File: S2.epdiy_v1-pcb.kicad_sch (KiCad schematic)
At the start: 87 parts, among them J1 USB_C_Receptacle_USB2.0, J2 Jack-DC, P1 CONN_02X13, SW1 RESET, SW2 BOOT, U1 MCP1700-1202E_SOT23, U11 TP4056, U2 ESP32-S2-WROVER, U3 QFN50P700X700X100-49N, U6 ED060XC5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

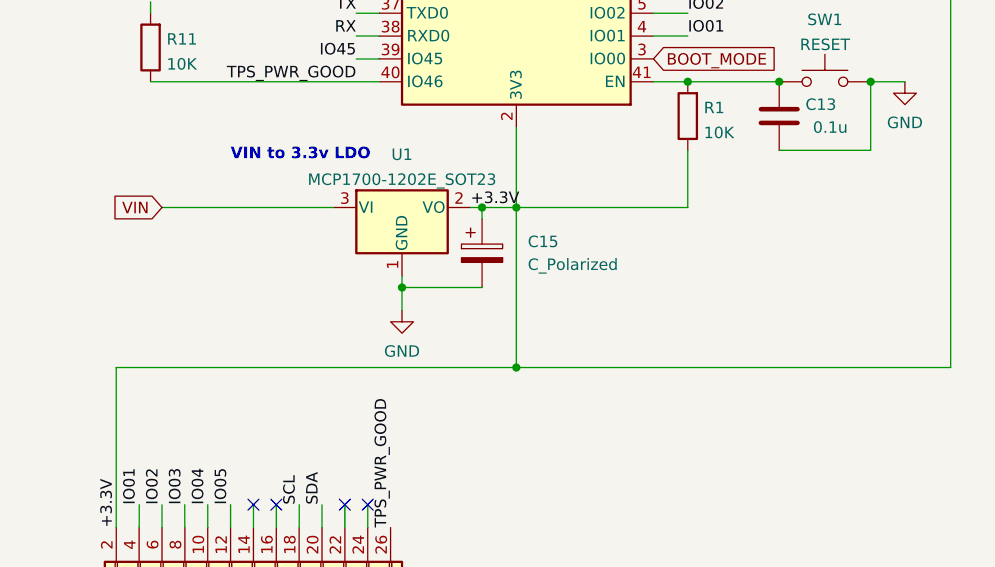
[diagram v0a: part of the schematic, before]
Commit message: Update LDO caps
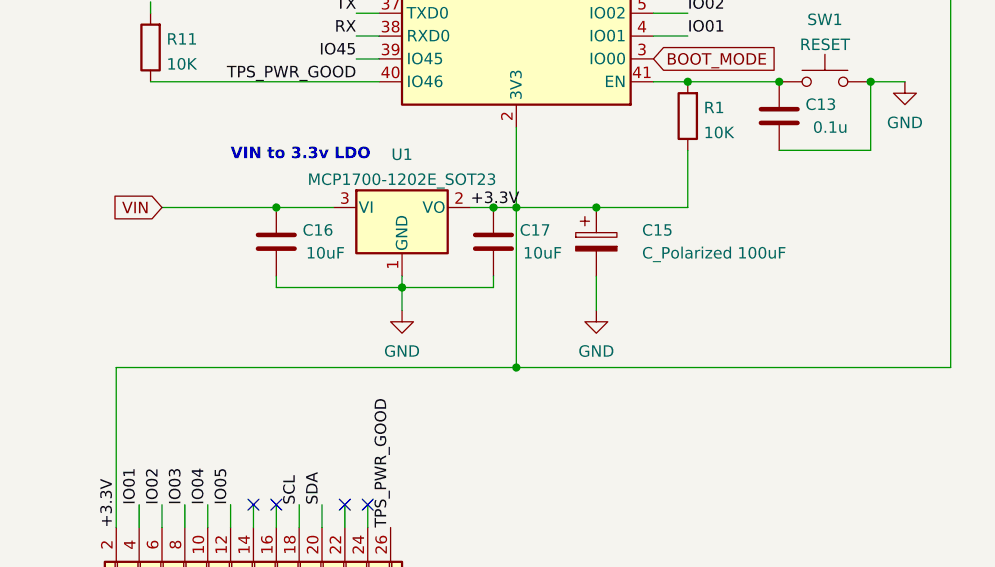
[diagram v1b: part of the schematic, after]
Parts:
- added C16, C17: 10uF, Capacitor_SMD:C_0805_2012Metric, symbol Device:C
- C15: value C_Polarized -> C_Polarized 100uF; footprint Capacitor_Tantalum_SMD:CP_EIA-7343-43_Kemet-X -> Capacitor_Tantalum_SMD:CP_EIA-3528-21_Kemet-B; LCSC C513339 -> C129289
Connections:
- net +3.3V: now also C17.1
- net GND: now also C16.2, C17.2
- net SW_VIN: now also C16.1
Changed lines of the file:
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@@
   (junction (at 309.88 226.06) (diameter 0) (color 0 0 0 0)
   )
+  (junction (at 129.54 105.41) (diameter 0) (color 0 0 0 0)
+  )
   (junction (at 326.39 71.12) (diameter 0) (color 0 0 0 0)
   )
@@
   (junction (at 341.63 177.8) (diameter 0) (color 0 0 0 0)
   )
+  (junction (at 140.97 105.41) (diameter 0) (color 0 0 0 0)
+  )
   (junction (at 339.09 146.05) (diameter 0) (color 0 0 0 0)
   )
@@
   (junction (at 320.04 146.05) (diameter 0) (color 0 0 0 0)
   )
-  (junction (at 128.27 105.41) (diameter 0) (color 0 0 0 0)
-  )
   (junction (at 321.31 214.63) (diameter 0) (color 0 0 0 0)
   )
@@
   (junction (at 120.65 232.41) (diameter 0) (color 0 0 0 0)
   )
+  (junction (at 105.41 105.41) (diameter 0) (color 0 0 0 0)
+  )
   (junction (at 227.33 185.42) (diameter 0) (color 0 0 0 0)
   )
@@
     (stroke (width 0) (type default) (color 0 0 0 0))
   )
-  (wire (pts (xy 151.13 105.41) (xy 132.08 105.41))
+  (wire (pts (xy 151.13 105.41) (xy 140.97 105.41))
     (stroke (width 0) (type default) (color 0 0 0 0))
   )
@@
     (stroke (width 0) (type default) (color 0 0 0 0))
   )
+  (wire (pts (xy 129.54 105.41) (xy 132.08 105.41))
+    (stroke (width 0) (type default) (color 0 0 0 0))
+  )
   (wire (pts (xy 220.98 170.18) (xy 220.98 177.8))
     (stroke (width 0) (type default) (color 0 0 0 0))
@@
     (stroke (width 0) (type default) (color 0 0 0 0))
   )
+  (wire (pts (xy 140.97 116.84) (xy 140.97 113.03))
+    (stroke (width 0) (type default) (color 0 0 0 0))
+  )
   (wire (pts (xy 303.53 154.94) (xy 303.53 144.78))
     (stroke (width 0) (type default) (color 0 0 0 0))
@@
     (stroke (width 0) (type default) (color 0 0 0 0))
   )
+  (wire (pts (xy 129.54 114.3) (xy 129.54 113.03))
+    (stroke (width 0) (type default) (color 0 0 0 0))
+  )
   (wire (pts (xy 151.13 83.82) (xy 147.32 83.82))
     (stroke (width 0) (type default) (color 0 0 0 0))
@@
     (stroke (width 0) (type default) (color 0 0 0 0))
   )
+  (wire (pts (xy 105.41 105.41) (xy 111.76 105.41))
+    (stroke (width 0) (type default) (color 0 0 0 0))
+  )
   (wire (pts (xy 114.3 232.41) (xy 120.65 232.41))
     (stroke (width 0) (type default) (color 0 0 0 0))
@@
     (stroke (width 0) (type default) (color 0 0 0 0))
   )
-  (wire (pts (xy 127 105.41) (xy 128.27 105.41))
+  (wire (pts (xy 127 105.41) (xy 129.54 105.41))
     (stroke (width 0) (type default) (color 0 0 0 0))
   )
@@
     (stroke (width 0) (type default) (color 0 0 0 0))
   )
+  (wire (pts (xy 119.38 114.3) (xy 105.41 114.3))
+    (stroke (width 0) (type default) (color 0 0 0 0))
+  )
   (wire (pts (xy 337.82 184.15) (xy 339.09 184.15))
     (stroke (width 0) (type default) (color 0 0 0 0))
@@
     (stroke (width 0) (type default) (color 0 0 0 0))
   )
+  (wire (pts (xy 140.97 105.41) (xy 132.08 105.41))
+    (stroke (width 0) (type default) (color 0 0 0 0))
+  )
   (wire (pts (xy 250.19 154.94) (xy 242.57 154.94))
     (stroke (width 0) (type default) (color 0 0 0 0))
@@
     (stroke (width 0) (type default) (color 0 0 0 0))
   )
+  (wire (pts (xy 105.41 114.3) (xy 105.41 113.03))
+    (stroke (width 0) (type default) (color 0 0 0 0))
+  )
   (wire (pts (xy 361.95 161.29) (xy 360.68 161.29))
     (stroke (width 0) (type default) (color 0 0 0 0))
@@
     (stroke (width 0) (type default) (color 0 0 0 0))
   )
-  (wire (pts (xy 119.38 114.3) (xy 128.27 114.3))
+  (wire (pts (xy 119.38 114.3) (xy 129.54 114.3))
     (stroke (width 0) (type default) (color 0 0 0 0))
   )
@@
     (stroke (width 0) (type default) (color 0 0 0 0))
   )
-  (wire (pts (xy 128.27 106.68) (xy 128.27 105.41))
-    (stroke (width 0) (type default) (color 0 0 0 0))
-  )
-  (wire (pts (xy 92.71 105.41) (xy 111.76 105.41))
+  (wire (pts (xy 92.71 105.41) (xy 105.41 105.41))
     (stroke (width 0) (type default) (color 0 0 0 0))
   )
@@
     (stroke (width 0) (type default) (color 0 0 0 0))
   )
-  (wire (pts (xy 128.27 105.41) (xy 132.08 105.41))
-    (stroke (width 0) (type default) (color 0 0 0 0))
-  )
   (wire (pts (xy 168.91 232.41) (xy 162.56 232.41))
     (stroke (width 0) (type default) (color 0 0 0 0))
@@
     (pin "2")
   )
+  (symbol (lib_id "power:GND") (at 140.97 116.84 0) (unit 1)
+    (in_bom yes) (on_board yes) (fields_autoplaced)
+    (property "Reference" "#PWR0111" (id 0) (at 140.97 123.19 0)
+      (effects (font (size 1.27 1.27)) hide)
+    )
+    (property "Value" "GND" (id 1) (at 140.97 121.4025 0))
+    (property "Footprint" "" (id 2) (at 140.97 116.84 0)
+      (effects (font (size 1.27 1.27)) hide)
+    )
+    (property "Datasheet" "" (id 3) (at 140.97 116.84 0)
+      (effects (font (size 1.27 1.27)) hide)
+    )
+    (pin "1")
+  )
   (symbol (lib_id "Device:LED") (at 334.01 74.93 90) (unit 1)
     (in_bom yes) (on_board yes) (fields_autoplaced)
@@
     (pin "2")
   )
-  (symbol (lib_id "Device:C_Polarized") (at 128.27 110.49 0) (unit 1)
-    (in_bom yes) (on_board yes)
-    (property "Reference" "C15" (id 0) (at 133.35 109.22 0)
-      (effects (font (size 1.27 1.27)) (justify left))
-    )
-    (property "Value" "C_Polarized" (id 1) (at 133.35 111.76 0)
-      (effects (font (size 1.27 1.27)) (justify left))
-    )
-    (property "Footprint" "Capacitor_Tantalum_SMD:CP_EIA-7343-43_Kemet-X" (id 2) (at 129.2352 114.3 0)
-      (effects (font (size 1.27 1.27)) hide)
-    )
-    (property "Datasheet" "https://datasheet.lcsc.com/lcsc/2004141707_KEMET-T491X477K010AT_C513339.pdf" (id 3) (at 128.27 110.49 0)
-      (effects (font (size 1.27 1.27)) hide)
-    )
-    (property "LCSC" "C513339" (id 4) (at 128.27 110.49 0)
-      (effects (font (size 1.27 1.27)) hide)
-    )
-    (pin "1")
-    (pin "2")
-  )
   (symbol (lib_id "Connector:Jack-DC") (at 229.87 85.09 0) (unit 1)
     (in_bom yes) (on_board yes) (fields_autoplaced)
@@
     (pin "1")
   )
+  (symbol (lib_id "Device:C") (at 105.41 109.22 0) (unit 1)
+    (in_bom yes) (on_board yes)
+    (property "Reference" "C16" (id 0) (at 111.76 107.95 0)
+      (effects (font (size 1.27 1.27)) (justify right))
+    )
+    (property "Value" "10uF" (id 1) (at 113.03 110.49 0)
+      (effects (font (size 1.27 1.27)) (justify right))
+    )
+    (property "Footprint" "Capacitor_SMD:C_0805_2012Metric" (id 2) (at 106.3752 113.03 0)
+      (effects (font (size 1.27 1.27)) hide)
+    )
+    (property "Datasheet" "~" (id 3) (at 105.41 109.22 0)
+      (effects (font (size 1.27 1.27)) hide)
+    )
+    (property "LCSC" "C15850" (id 4) (at 105.41 109.22 0)
+      (effects (font (size 1.27 1.27)) hide)
+    )
+    (pin "1")
+    (pin "2")
+  )
   (symbol (lib_id "power:GND") (at 331.47 59.69 0) (unit 1)
     (in_bom yes) (on_board yes) (fields_autoplaced)
@@
     )
   )
+  (symbol (lib_id "Device:C_Polarized") (at 140.97 109.22 0) (unit 1)
+    (in_bom yes) (on_board yes)
+    (property "Reference" "C15" (id 0) (at 146.05 107.95 0)
+      (effects (font (size 1.27 1.27)) (justify left))
+    )
+    (property "Value" "C_Polarized 100uF" (id 1) (at 146.05 110.49 0)
+      (effects (font (size 1.27 1.27)) (justify left))
+    )
+    (property "Footprint" "Capacitor_Tantalum_SMD:CP_EIA-3528-21_Kemet-B" (id 2) (at 141.9352 113.03 0)
+      (effects (font (size 1.27 1.27)) hide)
+    )
+    (property "Datasheet" "https://datasheet.lcsc.com/lcsc/2004141707_KEMET-T491X477K010AT_C513339.pdf" (id 3) (at 140.97 109.22 0)
+      (effects (font (size 1.27 1.27)) hide)
+    )
+    (property "LCSC" "C129289" (id 4) (at 140.97 109.22 0)
+      (effects (font (size 1.27 1.27)) hide)
+    )
+    (pin "1")
+    (pin "2")
+  )
+  (symbol (lib_id "Device:C") (at 129.54 109.22 0) (unit 1)
+    (in_bom yes) (on_board yes)
+    (property "Reference" "C17" (id 0) (at 135.89 107.95 0)
+      (effects (font (size 1.27 1.27)) (justify right))
+    )
+    (property "Value" "10uF" (id 1) (at 137.16 110.49 0)
+      (effects (font (size 1.27 1.27)) (justify right))
+    )
+    (property "Footprint" "Capacitor_SMD:C_0805_2012Metric" (id 2) (at 130.5052 113.03 0)
+      (effects (font (size 1.27 1.27)) hide)
+    )
+    (property "Datasheet" "~" (id 3) (at 129.54 109.22 0)
+      (effects (font (size 1.27 1.27)) hide)
+    )
+    (property "LCSC" "C15850" (id 4) (at 129.54 109.22 0)
+      (effects (font (size 1.27 1.27)) hide)
+    )
+    (pin "1")
+    (pin "2")
+  )
   (symbol (lib_id "Device:C") (at 325.12 53.34 180) (unit 1)
     (in_bom yes) (on_board yes)
@@
       (reference "#PWR0110") (unit 1) (value "GND") (footprint "")
     )
+    (path "/0470bf8c-51db-40be-bed4-b8b12f1552af"
+      (reference "#PWR0111") (unit 1) (value "GND") (footprint "")
+    )
     (path "/00000000-0000-0000-0000-000065e9a59c"
       (reference "#PWR0113") (unit 1) (value "GND") (footprint "")
@@
       (reference "C14") (unit 1) (value "0.1u") (footprint "Capacitor_SMD:C_0805_2012Metric")
     )
-    (path "/518dd289-dd09-499b-a959-5caca8e3196e"
-      (reference "C15") (unit 1) (value "C_Polarized") (footprint "Capacitor_Tantalum_SMD:CP_EIA-7343-43_Kemet-X")
+    (path "/c5e86d78-a80a-4d18-b60f-90ff58339b80"
+      (reference "C15") (unit 1) (value "C_Polarized 100uF") (footprint "Capacitor_Tantalum_SMD:CP_EIA-3528-21_Kemet-B")
+    )
+    (path "/871e96ce-ad88-41b6-8fea-2cbba569a65b"
+      (reference "C16") (unit 1) (value "10uF") (footprint "Capacitor_SMD:C_0805_2012Metric")
+    )
+    (path "/c7e86f17-c1d6-413f-ac80-eaff4dec286b"
+      (reference "C17") (unit 1) (value "10uF") (footprint "Capacitor_SMD:C_0805_2012Metric")
     )
     (path "/00000000-0000-0000-0000-00006783cbac"

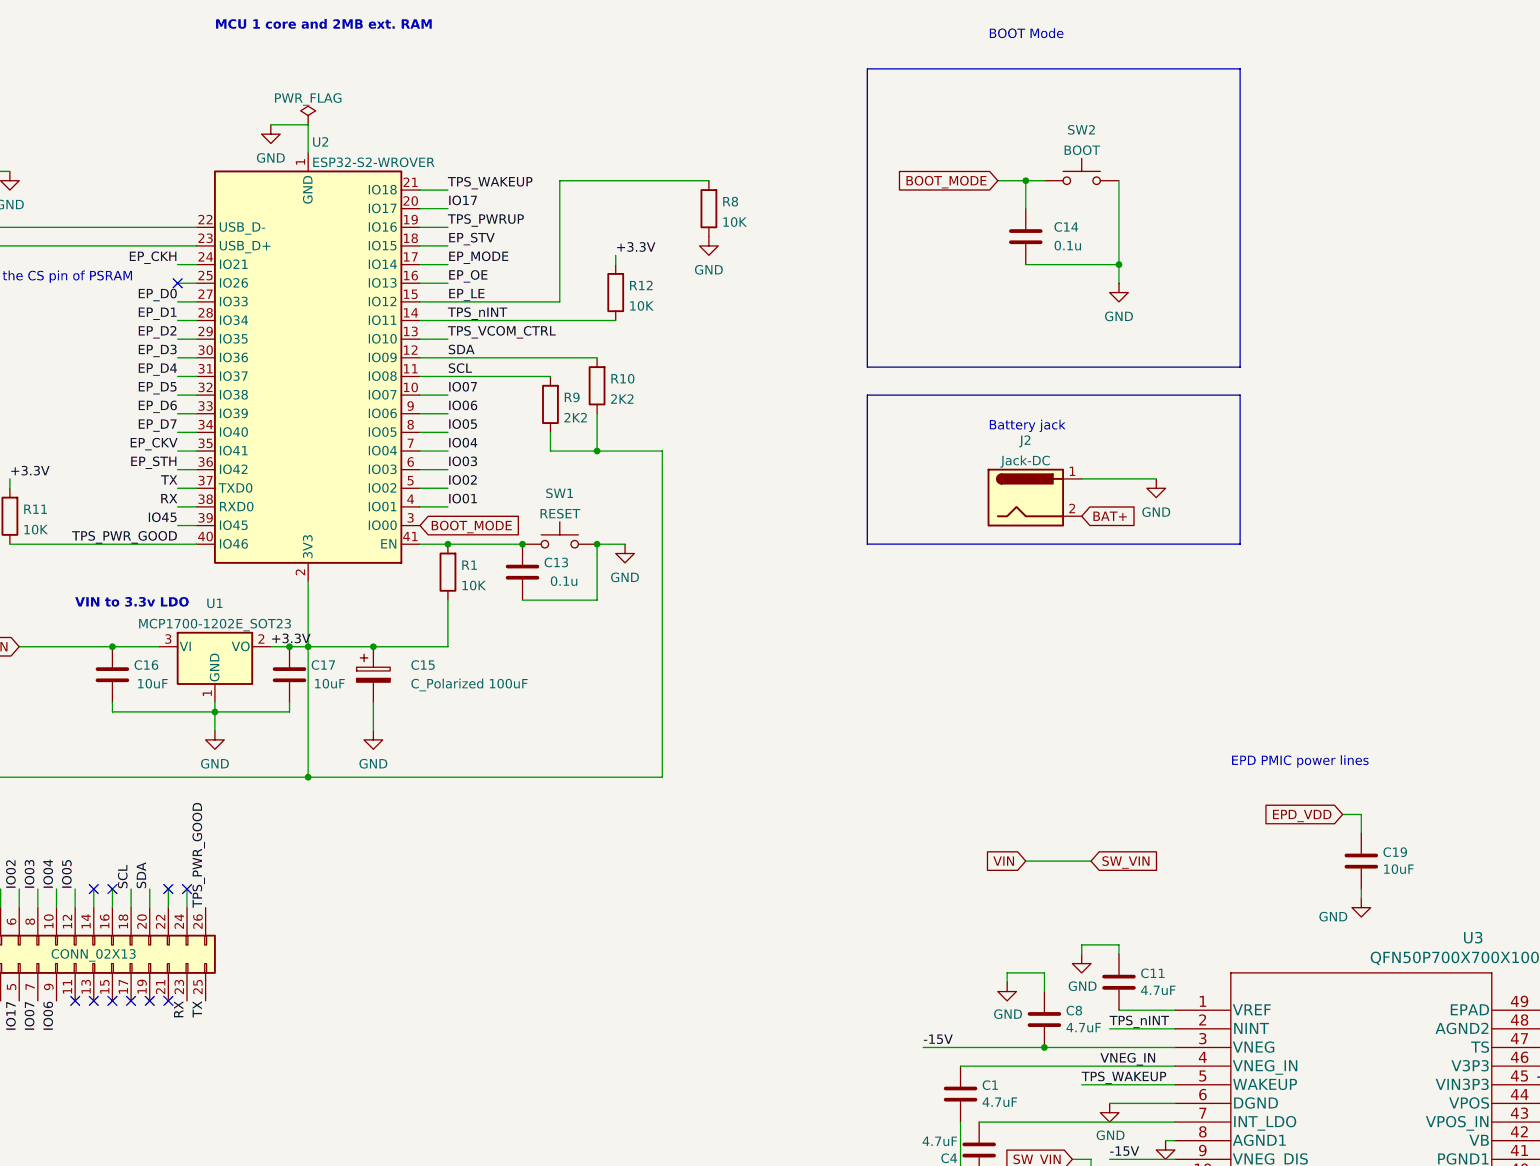
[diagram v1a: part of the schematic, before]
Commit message: Add DTS / RTS as suggested by Micke
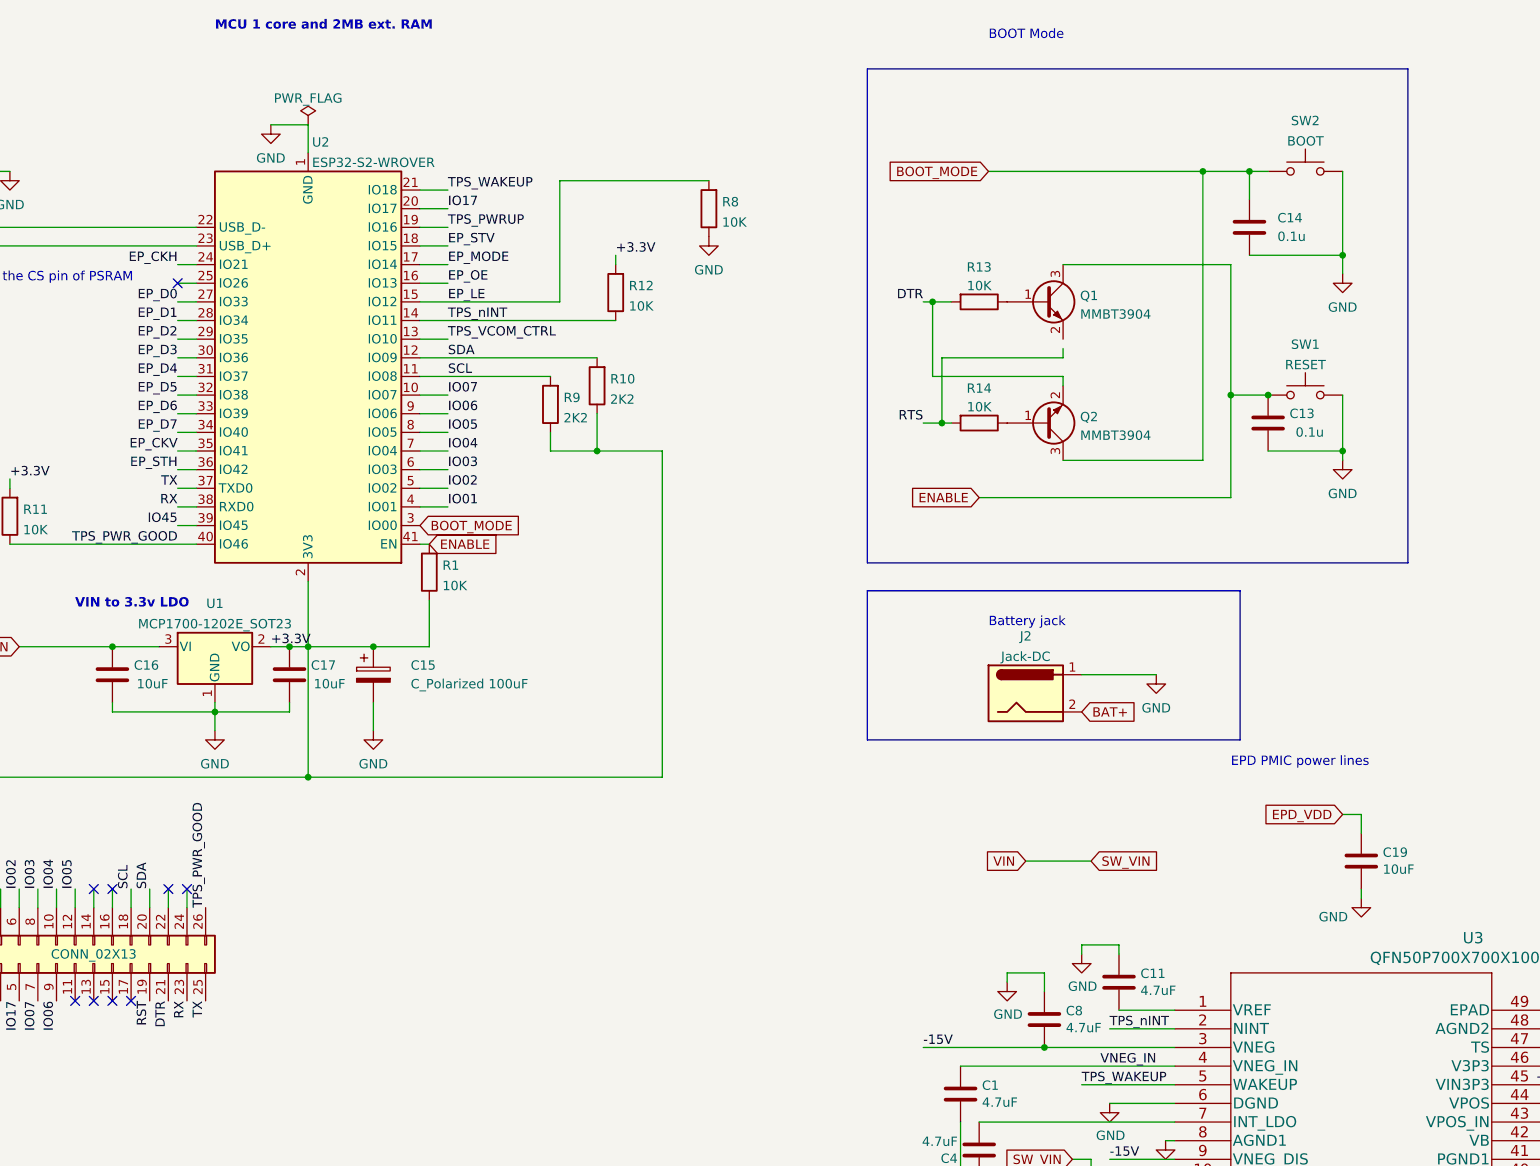
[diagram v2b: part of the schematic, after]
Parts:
- added Q1, Q2: MMBT3904, Package_TO_SOT_SMD:SOT-23, symbol Transistor_BJT:MMBT3904
- added R13, R14: 10K, Resistor_SMD:R_0603_1608Metric, symbol Device:R
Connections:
- net BOOT_MODE: now also Q2.3 (C)
- net RST: now reaches P1.19 (Pin_19)
- net DTR: now reaches P1.21 (Pin_21)
- net DTR: now also Q2.2 (E), R13.2
- net ENABLE: now reaches C13.1, R1.2, SW1.1, U2.41 (EN)
- net ENABLE: now also Q1.3 (C)
- new net: Q1.1 (B), R13.1
- new net: Q2.1 (B), R14.1
- new net RTS: R14.2
- no-connect marks 20 -> 18
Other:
- moved on the sheet: C14, J2, R1, SW2

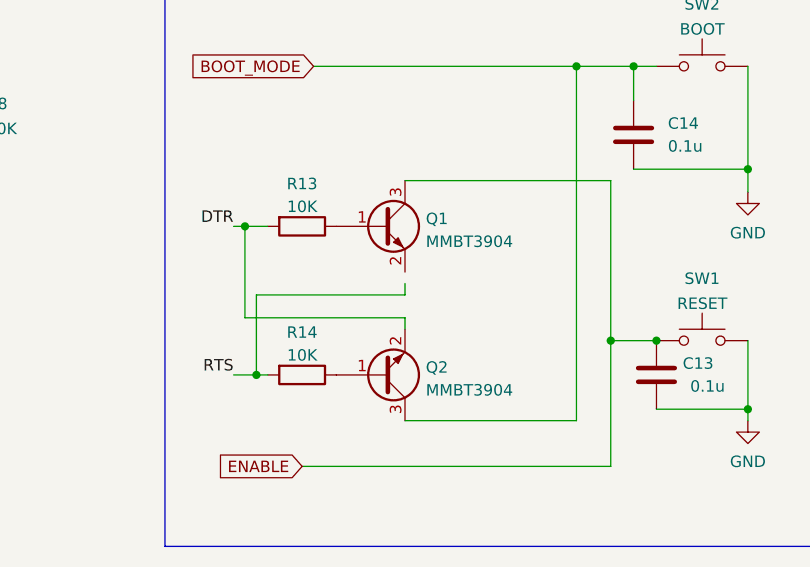
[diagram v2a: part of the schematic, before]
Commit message: Add DTS / RTS: Correction
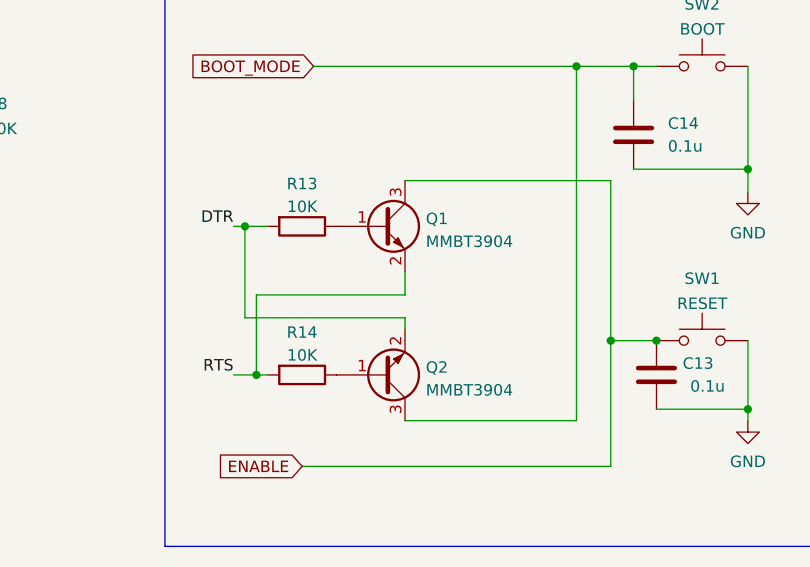
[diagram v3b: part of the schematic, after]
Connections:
- net RTS: now also Q1.2 (E)
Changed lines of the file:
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@@
     (stroke (width 0) (type default) (color 0 0 0 0))
   )
-  (wire (pts (xy 234.95 66.04) (xy 234.95 64.77))
+  (wire (pts (xy 234.95 63.5) (xy 234.95 66.04))
     (stroke (width 0) (type default) (color 0 0 0 0))
   )
